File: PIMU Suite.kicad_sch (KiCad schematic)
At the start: 5 parts, among them J1 Conn_01x05, U1 Teensy4.1, U2 MICROSD_SPI_OR_SDIO_CARD

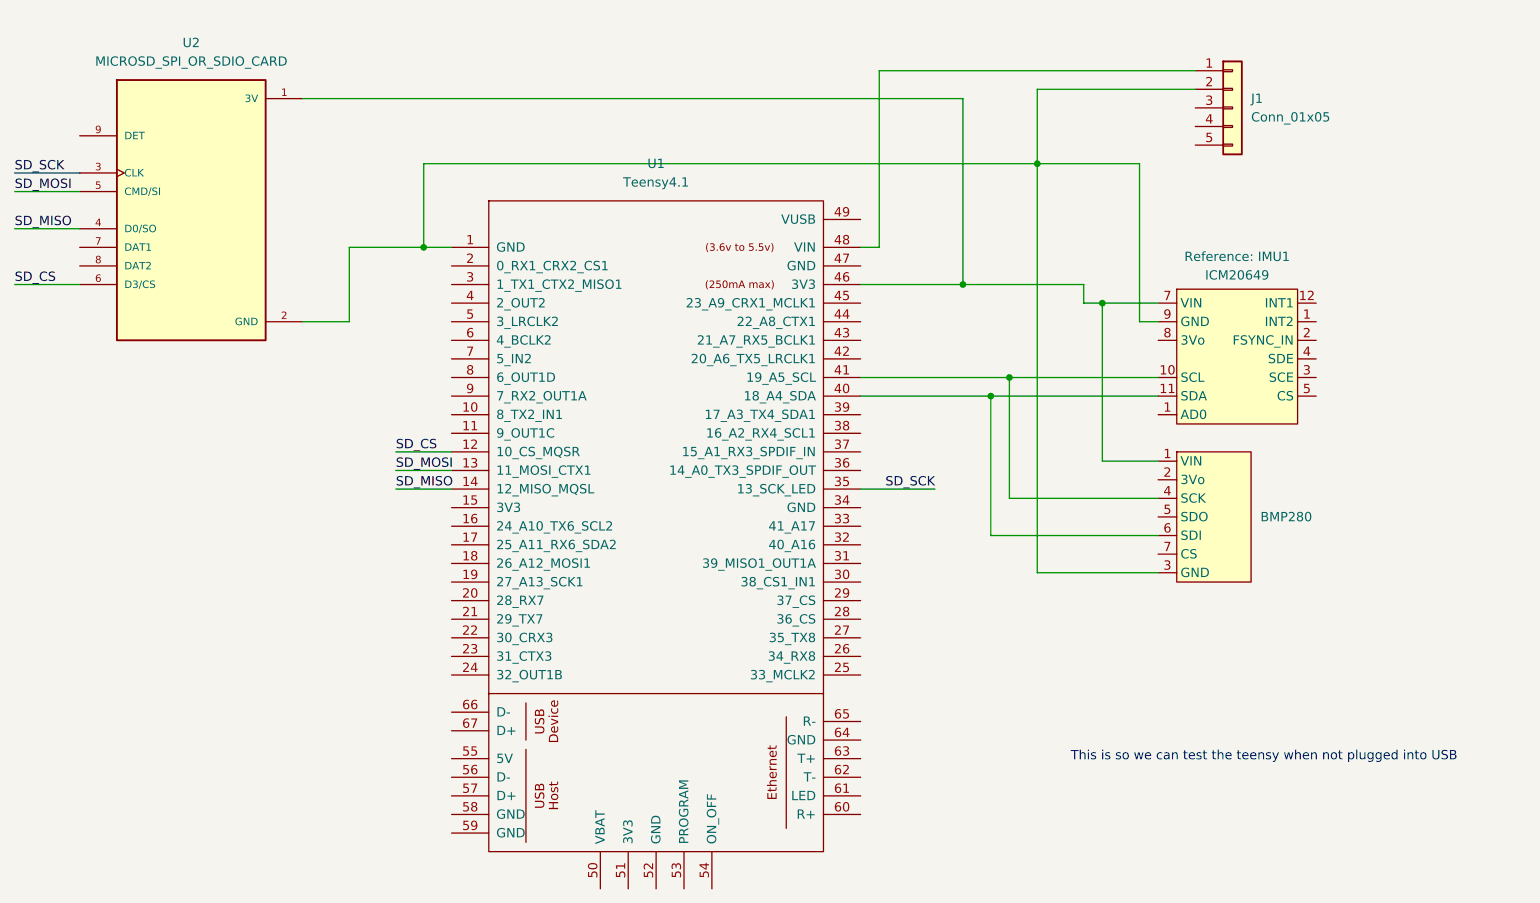
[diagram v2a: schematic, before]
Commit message: Actually use correct sensor
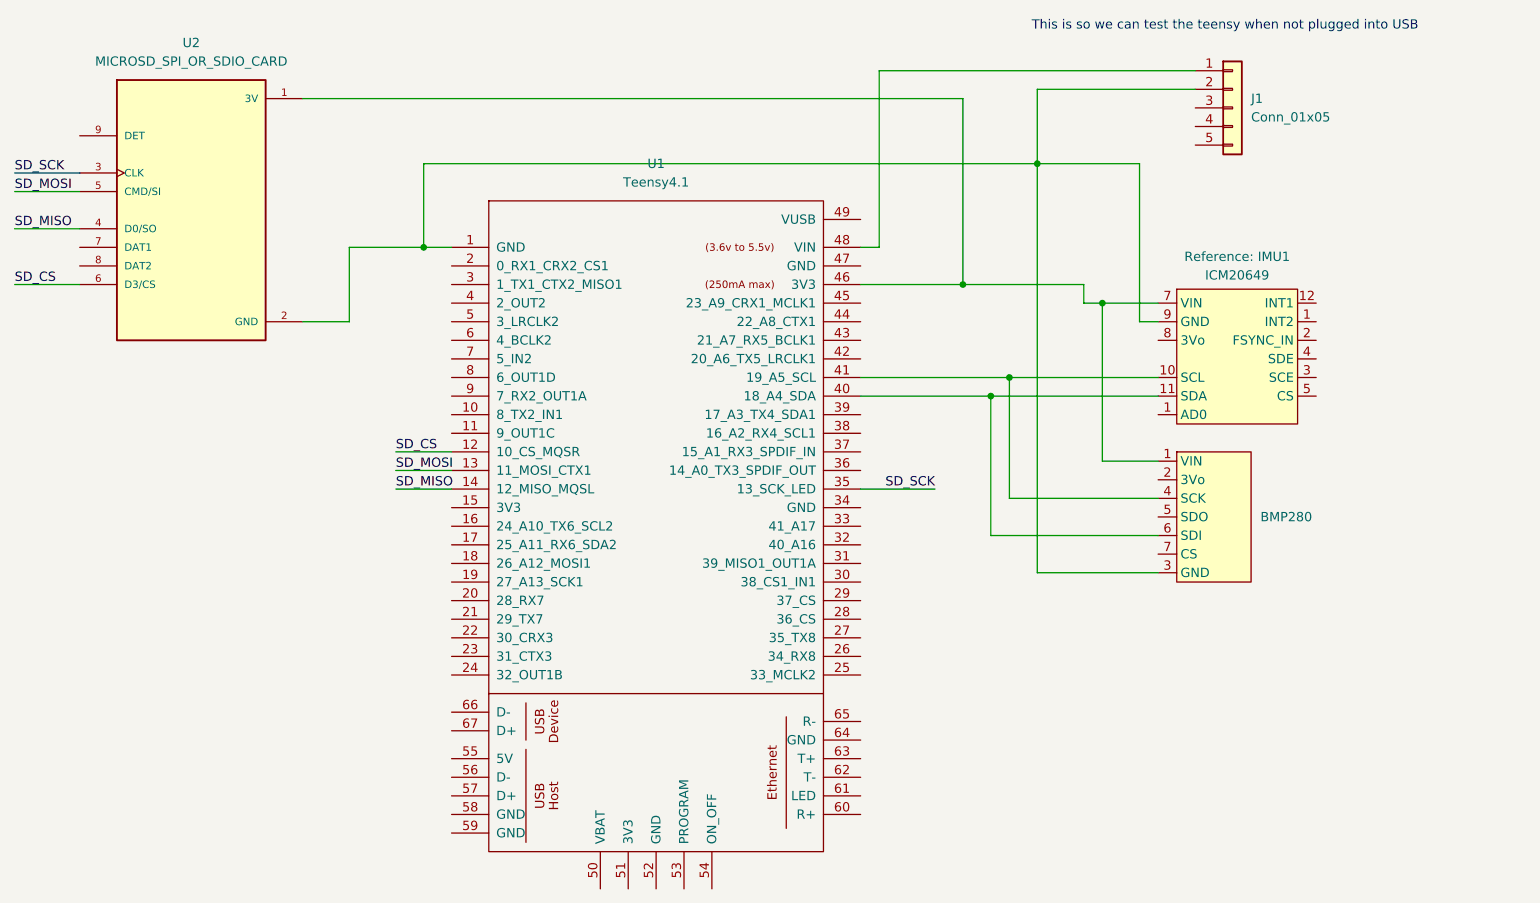
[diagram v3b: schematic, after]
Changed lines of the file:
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@@
 	(text "This is so we can test the teensy when not plugged into USB"
 		(exclude_from_sim no)
-		(at 227.838 129.286 0)
+		(at 222.504 29.464 0)
 		(effects
 			(font
